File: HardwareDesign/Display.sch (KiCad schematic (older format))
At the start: 30 parts, among them J601 Conn_01x12, U601 Upduino_3.0, U602 IDT7201, U603 74LVC245, U604 74LVC245

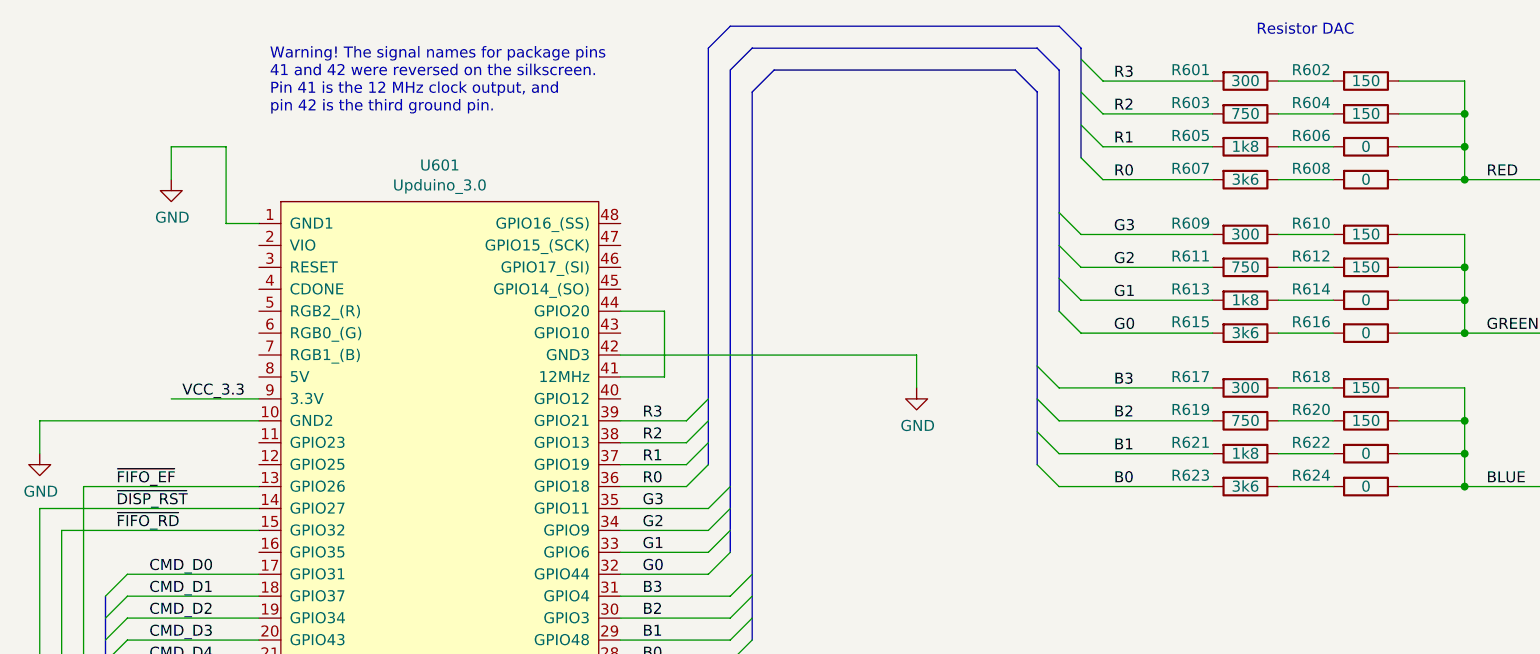
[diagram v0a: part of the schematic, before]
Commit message: improved resistor DAC values
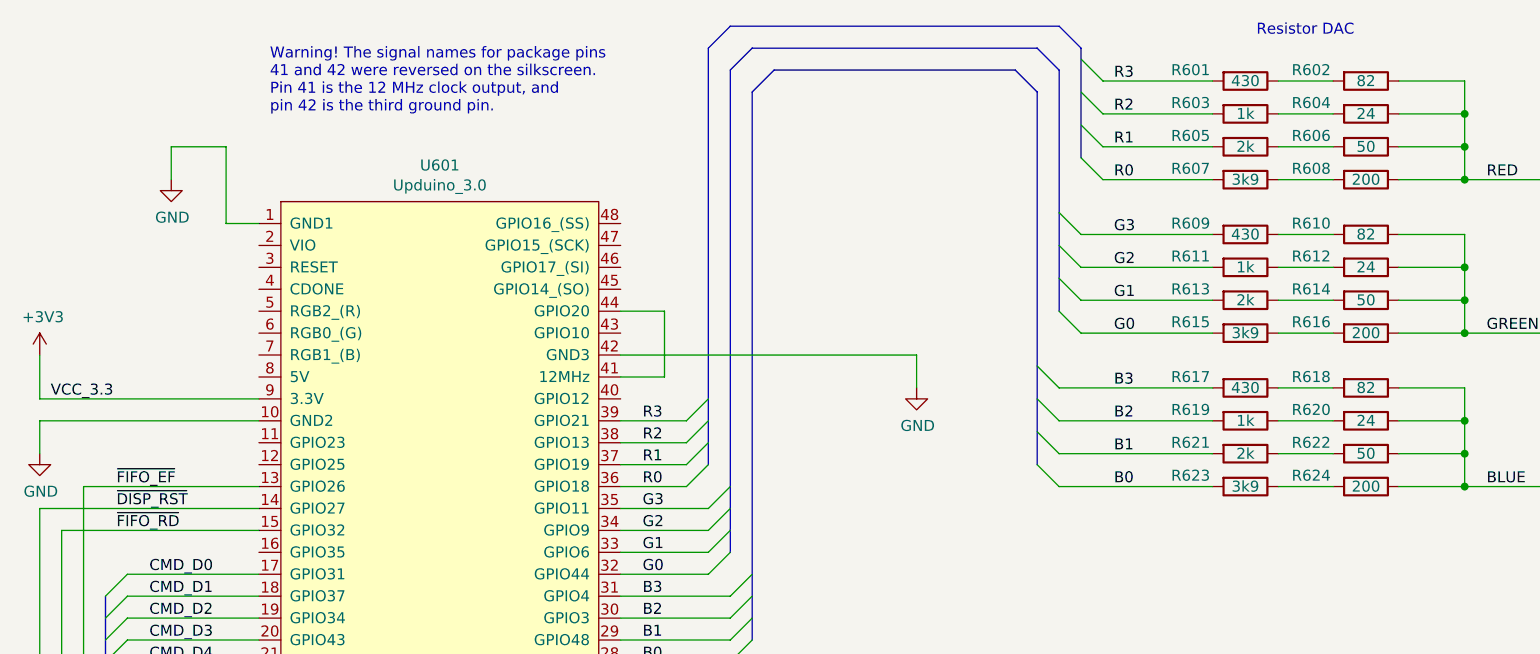
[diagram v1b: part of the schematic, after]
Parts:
- R601, R609, R617: value 300 -> 430
- R602, R610, R618: value 150 -> 82
- R603, R611, R619: value 750 -> 1k
- R604, R612, R620: value 150 -> 24
- R605, R613, R621: value 1k8 -> 2k
- R606, R614, R622: value 0 -> 50
- R607, R615, R623: value 3k6 -> 3k9
- R608, R616, R624: value 0 -> 200
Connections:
- net labels added: +3V3
- wire segments 195 -> 196
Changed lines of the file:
@@
 P 6300 1000
 F 0 "R603" V 6250 750 50  0000 C CNN
-F 1 "750" V 6300 1000 50  0000 C CNN
+F 1 "1k" V 6300 1000 50  0000 C CNN
 F 2 "Resistor_THT:R_Axial_DIN0204_L3.6mm_D1.6mm_P7.62mm_Horizontal" V 6230 1000 50  0001 C CNN
 F 3 "" H 6300 1000 50  0001 C CNN
@@
 P 6300 850
 F 0 "R601" V 6250 600 50  0000 C CNN
-F 1 "300" V 6300 850 50  0000 C CNN
+F 1 "430" V 6300 850 50  0000 C CNN
 F 2 "Resistor_THT:R_Axial_DIN0204_L3.6mm_D1.6mm_P7.62mm_Horizontal" V 6230 850 50  0001 C CNN
 F 3 "" H 6300 850 50  0001 C CNN
@@
 P 6850 1000
 F 0 "R604" V 6800 750 50  0000 C CNN
-F 1 "150" V 6850 1000 50  0000 C CNN
+F 1 "24" V 6850 1000 50  0000 C CNN
 F 2 "Resistor_THT:R_Axial_DIN0204_L3.6mm_D1.6mm_P7.62mm_Horizontal" V 6780 1000 50  0001 C CNN
 F 3 "" H 6850 1000 50  0001 C CNN
@@
 P 6850 850
 F 0 "R602" V 6800 600 50  0000 C CNN
-F 1 "150" V 6850 850 50  0000 C CNN
+F 1 "82" V 6850 850 50  0000 C CNN
 F 2 "Resistor_THT:R_Axial_DIN0204_L3.6mm_D1.6mm_P7.62mm_Horizontal" V 6780 850 50  0001 C CNN
 F 3 "" H 6850 850 50  0001 C CNN
@@
 P 6300 1300
 F 0 "R607" V 6250 1050 50  0000 C CNN
-F 1 "3k6" V 6300 1300 50  0000 C CNN
+F 1 "3k9" V 6300 1300 50  0000 C CNN
 F 2 "Resistor_THT:R_Axial_DIN0204_L3.6mm_D1.6mm_P7.62mm_Horizontal" V 6230 1300 50  0001 C CNN
 F 3 "" H 6300 1300 50  0001 C CNN
@@
 P 6300 1150
 F 0 "R605" V 6250 900 50  0000 C CNN
-F 1 "1k8" V 6300 1150 50  0000 C CNN
+F 1 "2k" V 6300 1150 50  0000 C CNN
 F 2 "Resistor_THT:R_Axial_DIN0204_L3.6mm_D1.6mm_P7.62mm_Horizontal" V 6230 1150 50  0001 C CNN
 F 3 "" H 6300 1150 50  0001 C CNN
@@
 P 6850 1300
 F 0 "R608" V 6800 1050 50  0000 C CNN
-F 1 "0" V 6850 1300 50  0000 C CNN
+F 1 "200" V 6850 1300 50  0000 C CNN
 F 2 "Resistor_THT:R_Axial_DIN0204_L3.6mm_D1.6mm_P7.62mm_Horizontal" V 6780 1300 50  0001 C CNN
 F 3 "" H 6850 1300 50  0001 C CNN
@@
 P 6850 1150
 F 0 "R606" V 6800 900 50  0000 C CNN
-F 1 "0" V 6850 1150 50  0000 C CNN
+F 1 "50" V 6850 1150 50  0000 C CNN
 F 2 "Resistor_THT:R_Axial_DIN0204_L3.6mm_D1.6mm_P7.62mm_Horizontal" V 6780 1150 50  0001 C CNN
 F 3 "" H 6850 1150 50  0001 C CNN
@@
 P 6300 1700
 F 0 "R611" V 6250 1450 50  0000 C CNN
-F 1 "750" V 6300 1700 50  0000 C CNN
+F 1 "1k" V 6300 1700 50  0000 C CNN
 F 2 "Resistor_THT:R_Axial_DIN0204_L3.6mm_D1.6mm_P7.62mm_Horizontal" V 6230 1700 50  0001 C CNN
 F 3 "" H 6300 1700 50  0001 C CNN
@@
 P 6300 1550
 F 0 "R609" V 6250 1300 50  0000 C CNN
-F 1 "300" V 6300 1550 50  0000 C CNN
+F 1 "430" V 6300 1550 50  0000 C CNN
 F 2 "Resistor_THT:R_Axial_DIN0204_L3.6mm_D1.6mm_P7.62mm_Horizontal" V 6230 1550 50  0001 C CNN
 F 3 "" H 6300 1550 50  0001 C CNN
@@
 P 6850 1700
 F 0 "R612" V 6800 1450 50  0000 C CNN
-F 1 "150" V 6850 1700 50  0000 C CNN
+F 1 "24" V 6850 1700 50  0000 C CNN
 F 2 "Resistor_THT:R_Axial_DIN0204_L3.6mm_D1.6mm_P7.62mm_Horizontal" V 6780 1700 50  0001 C CNN
 F 3 "" H 6850 1700 50  0001 C CNN
@@
 P 6850 1550
 F 0 "R610" V 6800 1300 50  0000 C CNN
-F 1 "150" V 6850 1550 50  0000 C CNN
+F 1 "82" V 6850 1550 50  0000 C CNN
 F 2 "Resistor_THT:R_Axial_DIN0204_L3.6mm_D1.6mm_P7.62mm_Horizontal" V 6780 1550 50  0001 C CNN
 F 3 "" H 6850 1550 50  0001 C CNN
@@
 P 6300 2000
 F 0 "R615" V 6250 1750 50  0000 C CNN
-F 1 "3k6" V 6300 2000 50  0000 C CNN
+F 1 "3k9" V 6300 2000 50  0000 C CNN
 F 2 "Resistor_THT:R_Axial_DIN0204_L3.6mm_D1.6mm_P7.62mm_Horizontal" V 6230 2000 50  0001 C CNN
 F 3 "" H 6300 2000 50  0001 C CNN
@@
 P 6300 1850
 F 0 "R613" V 6250 1600 50  0000 C CNN
-F 1 "1k8" V 6300 1850 50  0000 C CNN
+F 1 "2k" V 6300 1850 50  0000 C CNN
 F 2 "Resistor_THT:R_Axial_DIN0204_L3.6mm_D1.6mm_P7.62mm_Horizontal" V 6230 1850 50  0001 C CNN
 F 3 "" H 6300 1850 50  0001 C CNN
@@
 P 6850 2000
 F 0 "R616" V 6800 1750 50  0000 C CNN
-F 1 "0" V 6850 2000 50  0000 C CNN
+F 1 "200" V 6850 2000 50  0000 C CNN
 F 2 "Resistor_THT:R_Axial_DIN0204_L3.6mm_D1.6mm_P7.62mm_Horizontal" V 6780 2000 50  0001 C CNN
 F 3 "" H 6850 2000 50  0001 C CNN
@@
 P 6850 1850
 F 0 "R614" V 6800 1600 50  0000 C CNN
-F 1 "0" V 6850 1850 50  0000 C CNN
+F 1 "50" V 6850 1850 50  0000 C CNN
 F 2 "Resistor_THT:R_Axial_DIN0204_L3.6mm_D1.6mm_P7.62mm_Horizontal" V 6780 1850 50  0001 C CNN
 F 3 "" H 6850 1850 50  0001 C CNN
@@
 P 6300 2400
 F 0 "R619" V 6250 2150 50  0000 C CNN
-F 1 "750" V 6300 2400 50  0000 C CNN
+F 1 "1k" V 6300 2400 50  0000 C CNN
 F 2 "Resistor_THT:R_Axial_DIN0204_L3.6mm_D1.6mm_P7.62mm_Horizontal" V 6230 2400 50  0001 C CNN
 F 3 "" H 6300 2400 50  0001 C CNN
@@
 P 6300 2250
 F 0 "R617" V 6250 2000 50  0000 C CNN
-F 1 "300" V 6300 2250 50  0000 C CNN
+F 1 "430" V 6300 2250 50  0000 C CNN
 F 2 "Resistor_THT:R_Axial_DIN0204_L3.6mm_D1.6mm_P7.62mm_Horizontal" V 6230 2250 50  0001 C CNN
 F 3 "" H 6300 2250 50  0001 C CNN
@@
 P 6850 2400
 F 0 "R620" V 6800 2150 50  0000 C CNN
-F 1 "150" V 6850 2400 50  0000 C CNN
+F 1 "24" V 6850 2400 50  0000 C CNN
 F 2 "Resistor_THT:R_Axial_DIN0204_L3.6mm_D1.6mm_P7.62mm_Horizontal" V 6780 2400 50  0001 C CNN
 F 3 "" H 6850 2400 50  0001 C CNN
@@
 P 6850 2250
 F 0 "R618" V 6800 2000 50  0000 C CNN
-F 1 "150" V 6850 2250 50  0000 C CNN
+F 1 "82" V 6850 2250 50  0000 C CNN
 F 2 "Resistor_THT:R_Axial_DIN0204_L3.6mm_D1.6mm_P7.62mm_Horizontal" V 6780 2250 50  0001 C CNN
 F 3 "" H 6850 2250 50  0001 C CNN
@@
 P 6300 2700
 F 0 "R623" V 6250 2450 50  0000 C CNN
-F 1 "3k6" V 6300 2700 50  0000 C CNN
+F 1 "3k9" V 6300 2700 50  0000 C CNN
 F 2 "Resistor_THT:R_Axial_DIN0204_L3.6mm_D1.6mm_P7.62mm_Horizontal" V 6230 2700 50  0001 C CNN
 F 3 "" H 6300 2700 50  0001 C CNN
@@
 P 6300 2550
 F 0 "R621" V 6250 2300 50  0000 C CNN
-F 1 "1k8" V 6300 2550 50  0000 C CNN
+F 1 "2k" V 6300 2550 50  0000 C CNN
 F 2 "Resistor_THT:R_Axial_DIN0204_L3.6mm_D1.6mm_P7.62mm_Horizontal" V 6230 2550 50  0001 C CNN
 F 3 "" H 6300 2550 50  0001 C CNN
@@
 P 6850 2700
 F 0 "R624" V 6800 2450 50  0000 C CNN
-F 1 "0" V 6850 2700 50  0000 C CNN
+F 1 "200" V 6850 2700 50  0000 C CNN
 F 2 "Resistor_THT:R_Axial_DIN0204_L3.6mm_D1.6mm_P7.62mm_Horizontal" V 6780 2700 50  0001 C CNN
 F 3 "" H 6850 2700 50  0001 C CNN
@@
 P 6850 2550
 F 0 "R622" V 6800 2300 50  0000 C CNN
-F 1 "0" V 6850 2550 50  0000 C CNN
+F 1 "50" V 6850 2550 50  0000 C CNN
 F 2 "Resistor_THT:R_Axial_DIN0204_L3.6mm_D1.6mm_P7.62mm_Horizontal" V 6780 2550 50  0001 C CNN
 F 3 "" H 6850 2550 50  0001 C CNN
@@
 Entry Wire Line
 	1100 3900 1200 3800
-Wire Wire Line
-	1800 2300 1400 2300
-Text Label 1450 2300 0    50   ~ 0
+Text Label 850  2300 0    50   ~ 0
 VCC_3.3
 Wire Wire Line
@@
 Text Notes 1450 8050 0    50   ~ 0
 The Arduino is just standing\nin for the host system for now
+$Comp
+L power:+3V3 #PWR?
+U 1 1 614BB16D
+P 800 2100
+F 0 "#PWR?" H 800 1950 50  0001 C CNN
+F 1 "+3V3" H 815 2273 50  0000 C CNN
+F 2 "" H 800 2100 50  0001 C CNN
+F 3 "" H 800 2100 50  0001 C CNN
+	1    800  2100
+	1    0    0    -1
+$EndComp
+Wire Wire Line
+	800  2300 800  2100
+Wire Wire Line
+	800  2300 1800 2300
 Wire Bus Line
 	3750 6050 3750 8700

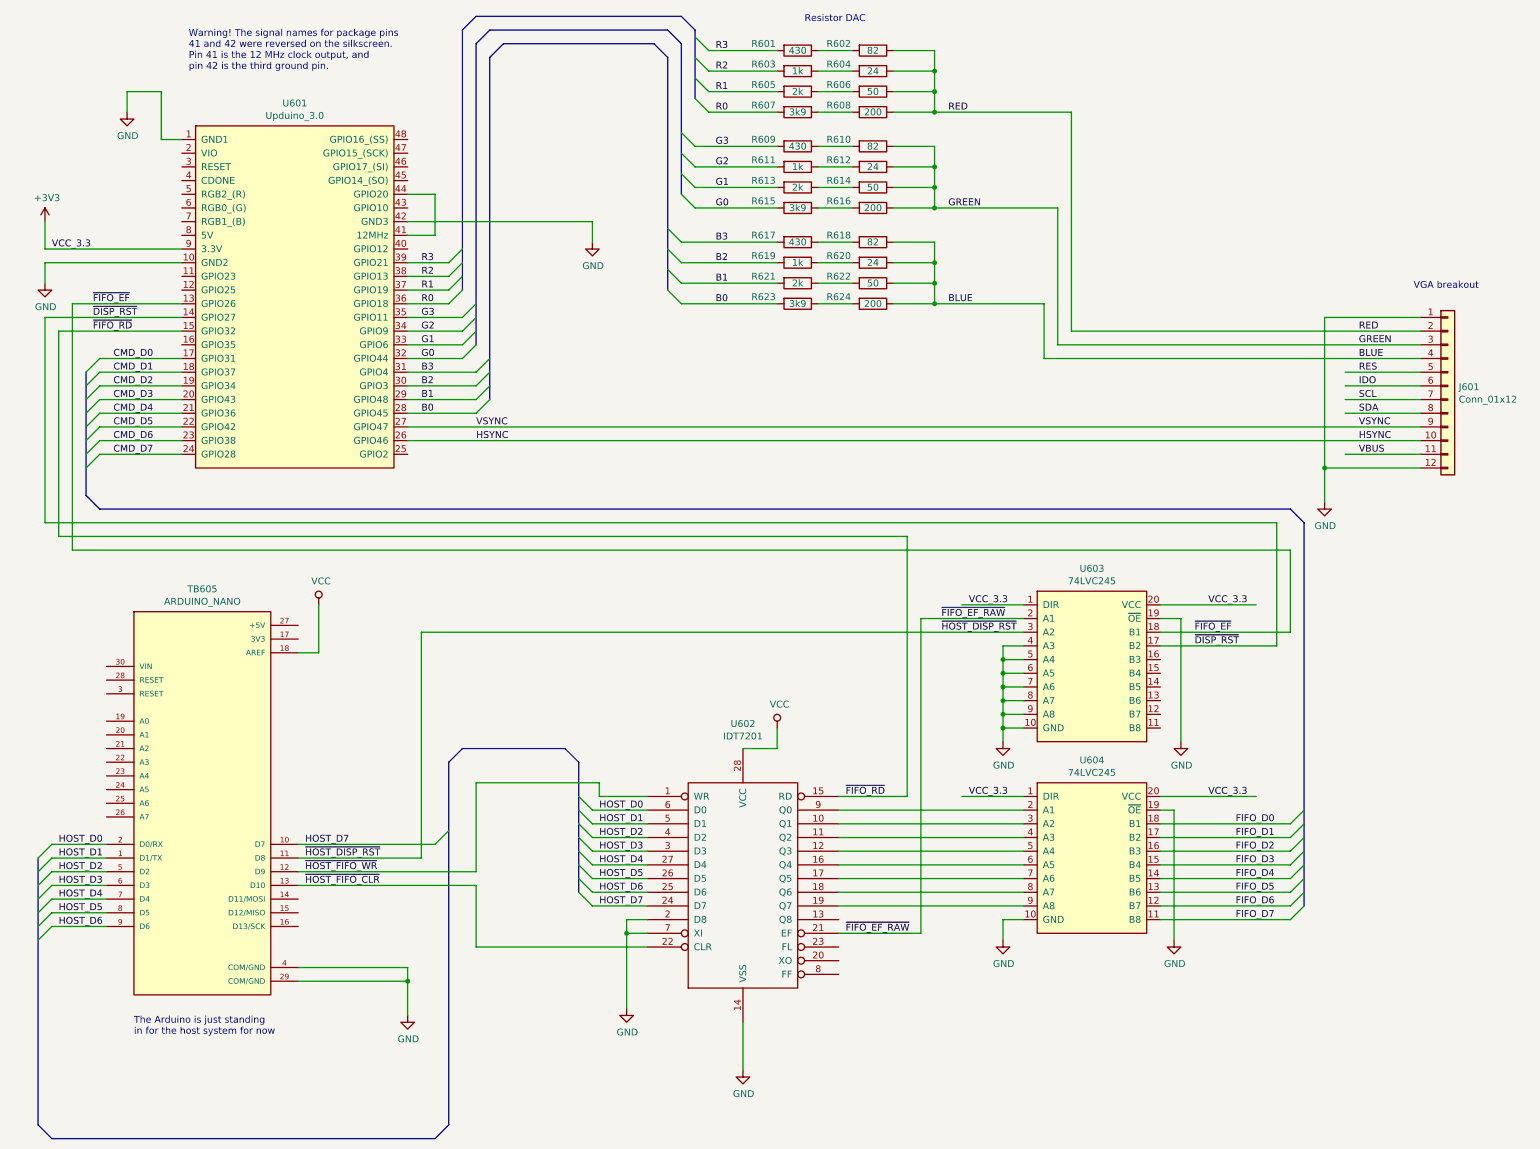
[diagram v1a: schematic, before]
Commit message: more tweaks/fixes to FIFO/FPGA interface
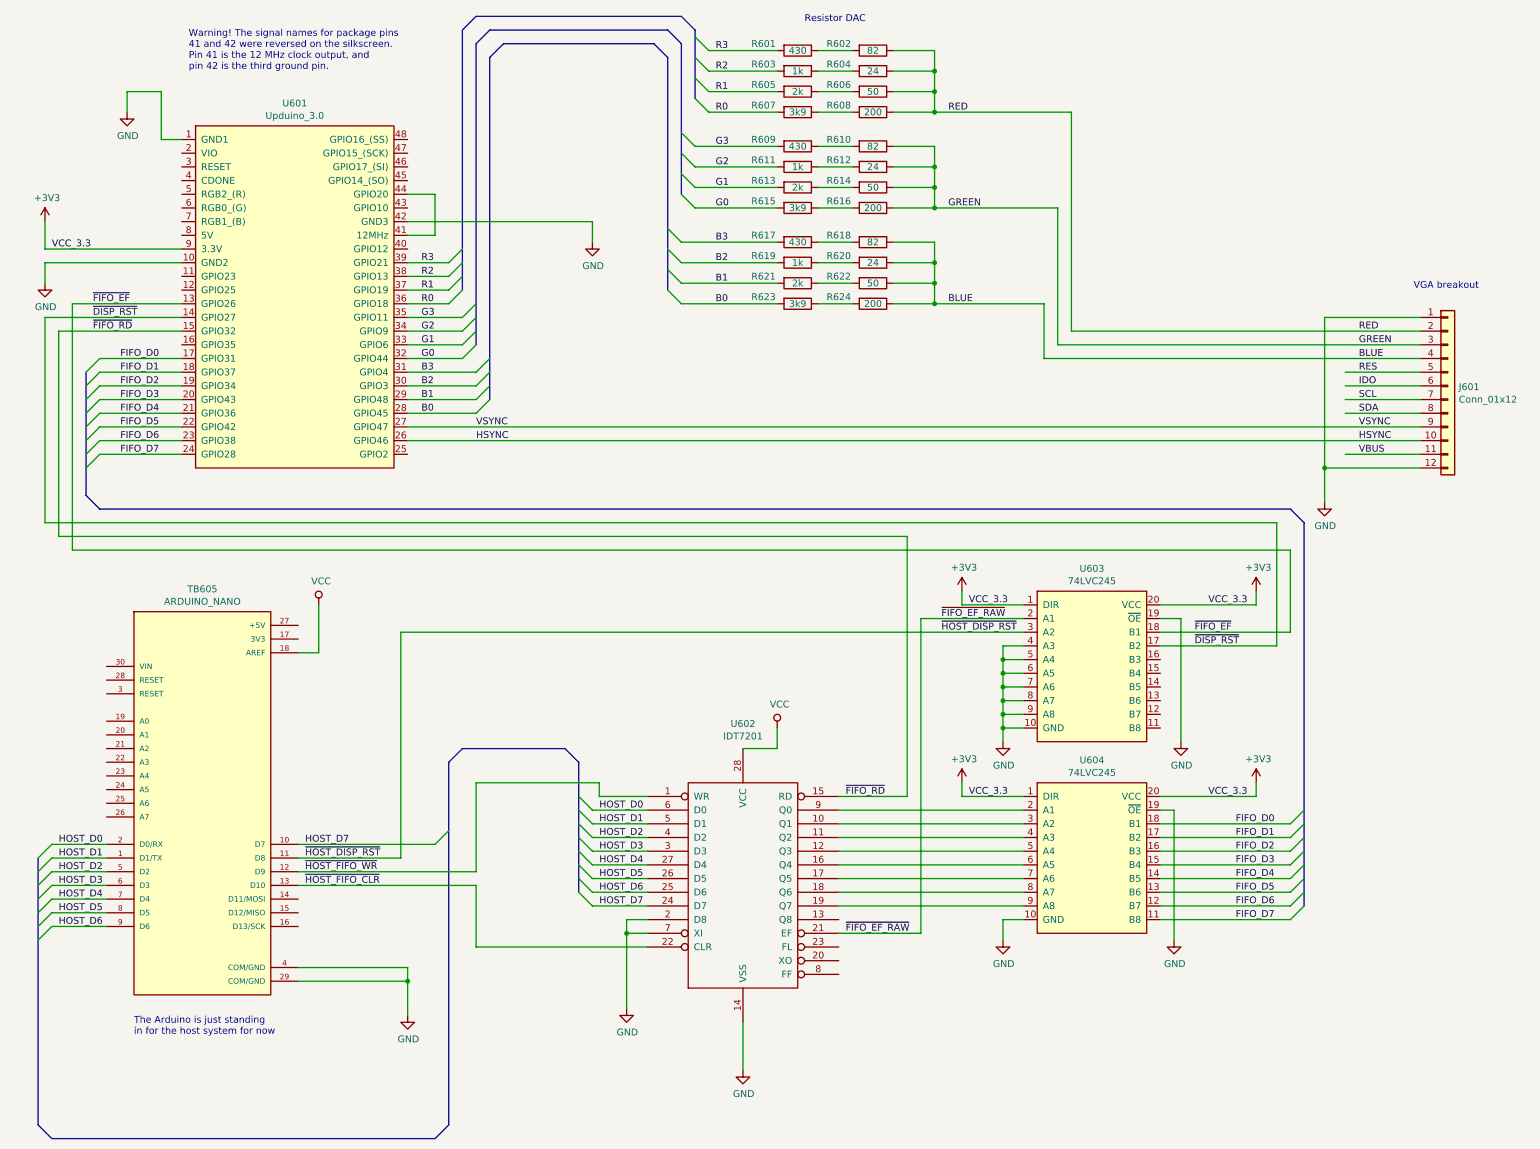
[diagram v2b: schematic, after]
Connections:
- net labels removed: CMD_D0, CMD_D1, CMD_D2, CMD_D3, CMD_D4, CMD_D5, CMD_D6, CMD_D7
- wire segments 196 -> 200
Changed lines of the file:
@@
 Wire Wire Line
 	1800 3800 1200 3800
-Text Label 1300 3100 0    50   ~ 0
-CMD_D0
-Text Label 1300 3200 0    50   ~ 0
-CMD_D1
-Text Label 1300 3300 0    50   ~ 0
-CMD_D2
-Text Label 1300 3400 0    50   ~ 0
-CMD_D3
-Text Label 1300 3500 0    50   ~ 0
-CMD_D4
-Text Label 1300 3600 0    50   ~ 0
-CMD_D5
-Text Label 1300 3700 0    50   ~ 0
-CMD_D6
-Text Label 1300 3800 0    50   ~ 0
-CMD_D7
 Entry Wire Line
 	1100 3200 1200 3100
@@
 	2650 6650 3650 6650
 Wire Wire Line
-	3550 5100 3550 6750
-Wire Wire Line
-	3550 6750 2650 6750
+	3400 5100 3400 6750
+Wire Wire Line
+	3400 6750 2650 6750
 Text Label 2700 6750 0    50   ~ 0
 ~HOST_DISP_RST~
@@
 ~FIFO_RD~
 Wire Wire Line
-	3550 5100 7950 5100
+	3400 5100 7950 5100
 Text Label 6650 7300 0    50   ~ 0
 ~FIFO_EF_RAW~
@@
 Wire Wire Line
 	800  2300 1800 2300
+$Comp
+L power:+3V3 #PWR?
+U 1 1 614F6E9B
+P 9650 4800
+F 0 "#PWR?" H 9650 4650 50  0001 C CNN
+F 1 "+3V3" H 9665 4973 50  0000 C CNN
+F 2 "" H 9650 4800 50  0001 C CNN
+F 3 "" H 9650 4800 50  0001 C CNN
+	1    9650 4800
+	1    0    0    -1
+$EndComp
+Wire Wire Line
+	9650 4800 9650 4900
+$Comp
+L power:+3V3 #PWR?
+U 1 1 61506165
+P 9650 6200
+F 0 "#PWR?" H 9650 6050 50  0001 C CNN
+F 1 "+3V3" H 9665 6373 50  0000 C CNN
+F 2 "" H 9650 6200 50  0001 C CNN
+F 3 "" H 9650 6200 50  0001 C CNN
+	1    9650 6200
+	1    0    0    -1
+$EndComp
+Wire Wire Line
+	9650 6200 9650 6300
+$Comp
+L power:+3V3 #PWR?
+U 1 1 61518B8A
+P 7500 4800
+F 0 "#PWR?" H 7500 4650 50  0001 C CNN
+F 1 "+3V3" H 7515 4973 50  0000 C CNN
+F 2 "" H 7500 4800 50  0001 C CNN
+F 3 "" H 7500 4800 50  0001 C CNN
+	1    7500 4800
+	1    0    0    -1
+$EndComp
+Wire Wire Line
+	7500 4800 7500 4900
+$Comp
+L power:+3V3 #PWR?
+U 1 1 6152CCB4
+P 7500 6200
+F 0 "#PWR?" H 7500 6050 50  0001 C CNN
+F 1 "+3V3" H 7515 6373 50  0000 C CNN
+F 2 "" H 7500 6200 50  0001 C CNN
+F 3 "" H 7500 6200 50  0001 C CNN
+	1    7500 6200
+	1    0    0    -1
+$EndComp
+Wire Wire Line
+	7500 6200 7500 6300
+Text Label 1350 3800 0    50   ~ 0
+FIFO_D7
+Text Label 1350 3700 0    50   ~ 0
+FIFO_D6
+Text Label 1350 3600 0    50   ~ 0
+FIFO_D5
+Text Label 1350 3500 0    50   ~ 0
+FIFO_D4
+Text Label 1350 3400 0    50   ~ 0
+FIFO_D3
+Text Label 1350 3300 0    50   ~ 0
+FIFO_D2
+Text Label 1350 3200 0    50   ~ 0
+FIFO_D1
+Text Label 1350 3100 0    50   ~ 0
+FIFO_D0
 Wire Bus Line
 	3750 6050 3750 8700
